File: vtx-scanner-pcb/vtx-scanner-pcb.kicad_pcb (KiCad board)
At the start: 2 copper layers, 24 parts, among them J1 Conn_01x06_Male, J2 Conn_01x08_Female, Q1 S8050, Q2 S8050, Q3 S8050, U1 RX5808, U2 AMS1117-3.3, U3 oskj-dc-dc, U4 AI-1027-TWT

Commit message: Started laying out PCB
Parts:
- added J3: SMA-J-P-H-RA-TH1, deets:SAMTEC_SMA-J-P-H-RA-TH1, B.Cu at (57.8, 40.8)
- added REF**: SSD1306, deets:SSD1306, F.Cu at (87.0, 46.4)
- C1, C2, C3, J1, J2, R1, R2, R3, U2, U3, U4: moved to B.Cu
- Q1, Q2, Q3: value S8050 -> MMSS8050-H-TP; footprint Package_TO_SOT_THT:TO-92_Inline -> digikey-footprints:SOT-23-3; moved to B.Cu
- S1, S2, S3, S4: value B3F-1000 -> FSM4JSMATR; footprint digikey-footprints:Switch_Tactile_THT_B3F-1xxx -> deets:Switch_Tactile_SMD_6x6mm
- moved U4 91.7 mm to (109.9, 39.4), turned to 180 degrees
- moved J2 76.2 mm to (94.6, 64.1), turned to 90 degrees
- moved Q3 68.6 mm to (112.4, 46.8), turned to 90 degrees
- moved A1 67.9 mm to (102.2, 78.1), turned to 90 degrees
- moved R7 63.7 mm to (94.6, 72.6), turned to 90 degrees
- moved R5 63.6 mm to (77.5, 72.8), turned to 90 degrees
- moved R6 62.5 mm to (77.5, 82.3), turned to 270 degrees
- moved R1 53.6 mm to (81.2, 131.2)
- moved C3 45.6 mm to (103.8, 91.4)
- moved R4 41.5 mm to (94.6, 82.3), turned to 270 degrees
- moved U2 37.8 mm to (96.5, 94.6), turned to 180 degrees
- moved C2 33.6 mm to (92.9, 143.3)
- moved R2 29.9 mm to (102.5, 105.9)
- moved U1 28.0 mm to (82.2, 48.5), turned to 0 degrees
- moved S1 26.5 mm to (85.7, 83.8)
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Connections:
- Q1 pad 1: /RTS -> Net-(Q1-Pad1)
- Q1 pad 2: Net-(Q1-Pad2) -> /RTS
- Q2 pad 1: /DTR -> Net-(Q2-Pad1)
- Q2 pad 2: Net-(Q2-Pad2) -> /DTR
- Q3 pad 1: -BATT -> /BUZZER
- Q3 pad 2: /BUZZER -> -BATT
- R1 pad 2: Net-(Q1-Pad2) -> Net-(Q1-Pad1)
- R2 pad 2: Net-(Q2-Pad2) -> Net-(Q2-Pad1)
- U1 pad 1: -BATT -> GNDA
- U1 pad 2: Net-(U1-Pad2) -> /ANT
- U1 pad 3: -BATT -> GNDA
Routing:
- net +5V: track 0.00 -> 136.9 mm, vias 0 -> 2
- net -BATT: track 0.00 -> 109.1 mm, vias 0 -> 1
- net /BUTTON_LEFT: track 0.00 -> 44.0 mm, vias 0 -> 1
- net /BUTTON_UP: track 0.00 -> 31.7 mm, vias 0 -> 1
- net /BUZZER: track 0.00 -> 25.3 mm
- net /BUTTON_DOWN: track 0.00 -> 24.5 mm, vias 0 -> 1
- net +3V3: track 0.00 -> 15.0 mm, vias 0 -> 1
- net GNDA: track 0.00 -> 13.3 mm
- net /ANT: track 0.00 -> 9.22 mm
- net /BUTTON_RIGHT: track 0.00 -> 9.10 mm
- net Net-(Q3-Pad3): track 0.00 -> 6.37 mm
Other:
- net class +5V added: clearance 0.2, trace_width 1.778, via_dia 0.8, via_drill 0.4
- net class GNDA_NN added: clearance 0.2, trace_width 0.75, via_dia 0.8, via_drill 0.4

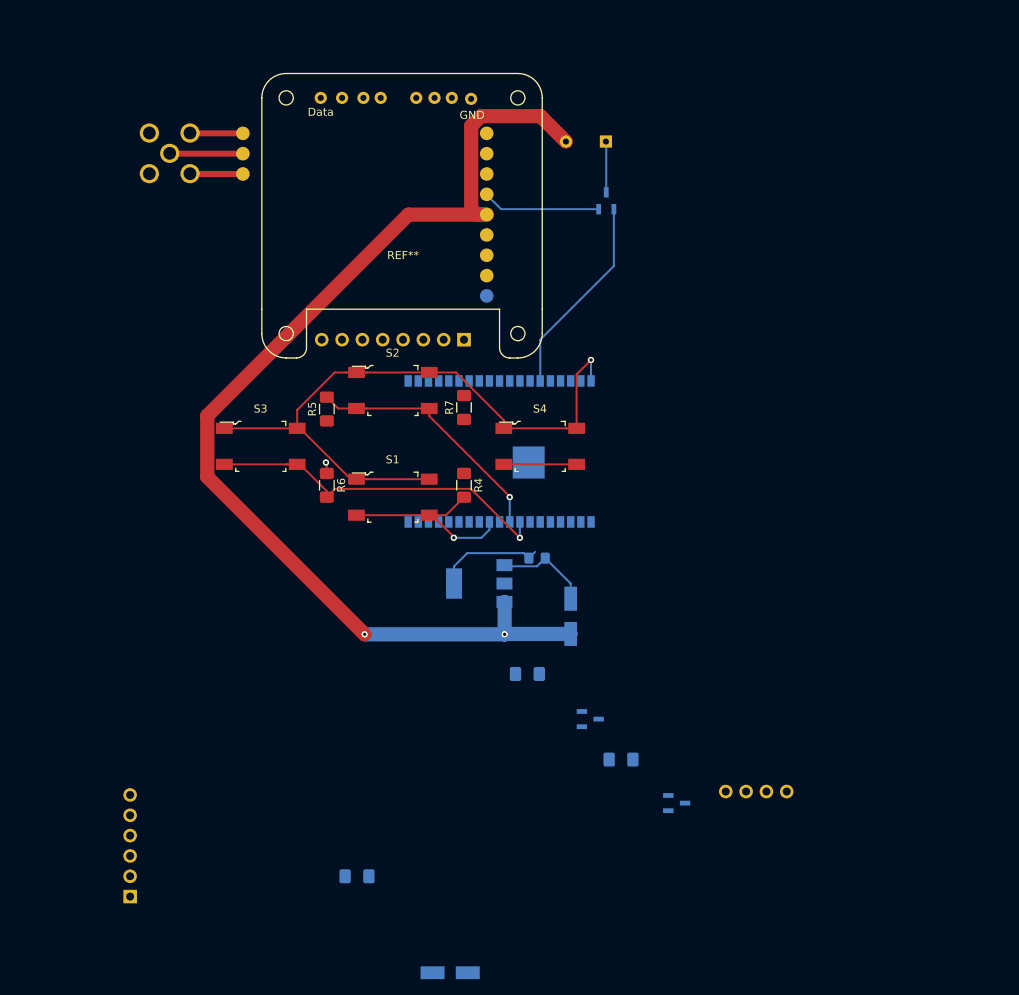
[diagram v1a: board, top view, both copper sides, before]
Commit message: Fully laid-out 4 layer PCB, the first!
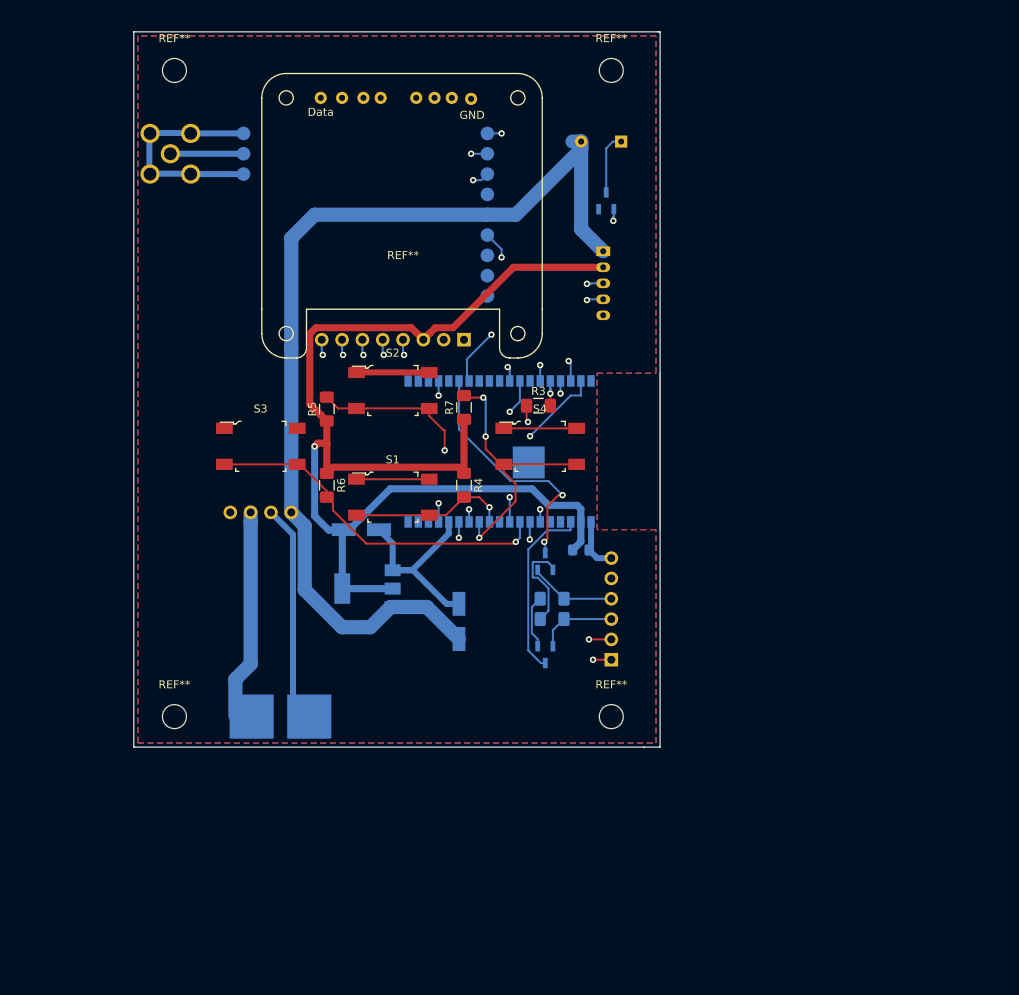
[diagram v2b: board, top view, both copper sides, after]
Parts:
- added J4: Conn_01x05, Connector_JST:JST_PH_S5B-PH-K_1x05_P2.00mm_Horizontal, B.Cu at (112.0, 53.1)
- added J5: XT60-M, deets:AMASS_XT60-M-SIDE-MOUNT, B.Cu at (71.7, 111.3)
- added REF**: MountingHole_3mm, MountingHole:MountingHole_3mm, F.Cu at (58.4, 30.5)
- added REF**: MountingHole_3mm, MountingHole:MountingHole_3mm, F.Cu at (113.0, 30.5)
- added REF**: MountingHole_3mm, MountingHole:MountingHole_3mm, F.Cu at (113.0, 111.3)
- added REF**: MountingHole_3mm, MountingHole:MountingHole_3mm, F.Cu at (58.4, 111.3)
- R3: moved to F.Cu
- moved J1 67.0 mm to (113.0, 104.1)
- moved U3 64.3 mm to (69.2, 94.6), turned to 180 degrees
- moved C2 56.5 mm to (81.8, 87.9)
- moved R3 45.4 mm to (103.9, 72.4)
- moved R1 42.4 mm to (105.6, 96.5), turned to 180 degrees
- moved Q1 24.8 mm to (104.8, 103.5), turned to 270 degrees
- moved Q2 20.5 mm to (104.8, 91.9), turned to 90 degrees
- moved C1 14.0 mm to (94.0, 99.4)
- moved U2 14.0 mm to (82.5, 95.2)
- moved R2 7.52 mm to (105.6, 99.1), turned to 180 degrees
- moved C3 5.56 mm to (109.2, 90.4)
- moved U4 1.91 mm to (111.8, 39.4)
- moved J3 0.10 mm to (57.9, 40.9)
- moved U1 0.08 mm to (82.3, 48.5)
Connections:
- A1 pad 26: Net-(A1-Pad26) -> /EXP1
- A1 pad 7: Net-(A1-Pad7) -> /EXP2
- J3 pad 2: GNDA -> -BATT
- J3 pad 3: GNDA -> -BATT
- J3 pad 4: GNDA -> -BATT
- J3 pad 5: GNDA -> -BATT
- U1 pad 1: GNDA -> -BATT
- U1 pad 3: GNDA -> -BATT
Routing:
- net +3V3: track 15.0 -> 151.7 mm
- net /VRX_DATA: track 0.00 -> 59.2 mm, vias 0 -> 2
- net /VRX_CS: track 0.00 -> 54.3 mm, vias 0 -> 2
- net /VRX_CLOCK: track 0.00 -> 46.6 mm, vias 0 -> 2
- net /SSD1306_DATA: track 0.00 -> 43.0 mm, vias 0 -> 2
- net /RX: track 0.00 -> 41.5 mm, vias 0 -> 2
- net /VRX_RSSI: track 0.00 -> 38.6 mm, vias 0 -> 2
- net /EXP2: track 0.00 -> 37.2 mm, vias 0 -> 2
- net /TX: track 0.00 -> 35.2 mm, vias 0 -> 2
- net /IO0: track 0.00 -> 30.9 mm, vias 0 -> 2
- net /SSD1306_CLK: track 0.00 -> 30.1 mm, vias 0 -> 2
- net +BATT: track 0.00 -> 26.2 mm
- net /BUTTON_RIGHT: track 9.10 -> 34.9 mm, vias 0 -> 3
- net /SSD1306_CS: track 0.00 -> 25.4 mm, vias 0 -> 2
- net /EXP1: track 0.00 -> 23.8 mm, vias 0 -> 2
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- added copper zone on B.Cu, net -BATT
- added copper zone on F.Cu, net -BATT
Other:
- board outline added: 65.8 x 89.4 mm
- copper layers 2 -> 4
- net class +3.3V added: clearance 0.2, trace_width 0.889, via_dia 0.8, via_drill 0.4

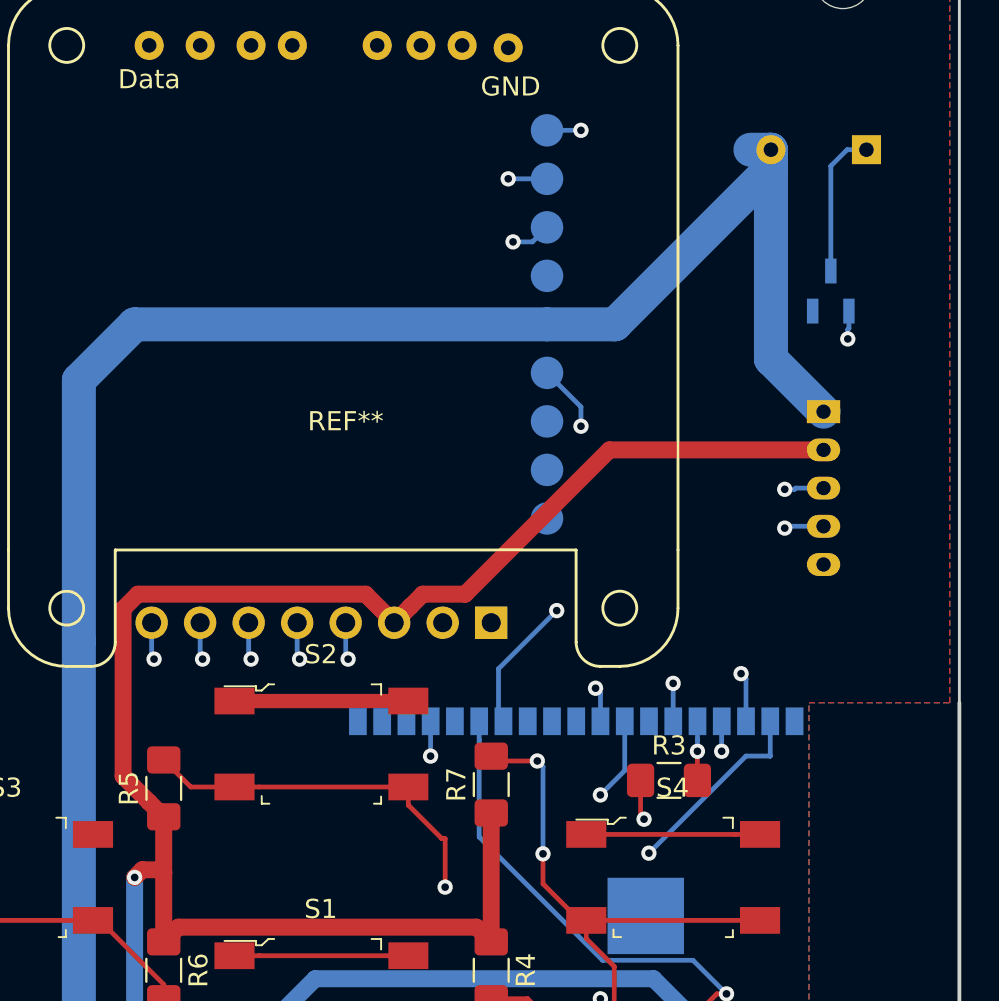
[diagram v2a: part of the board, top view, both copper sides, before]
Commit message: Re-organised a couple of power lines
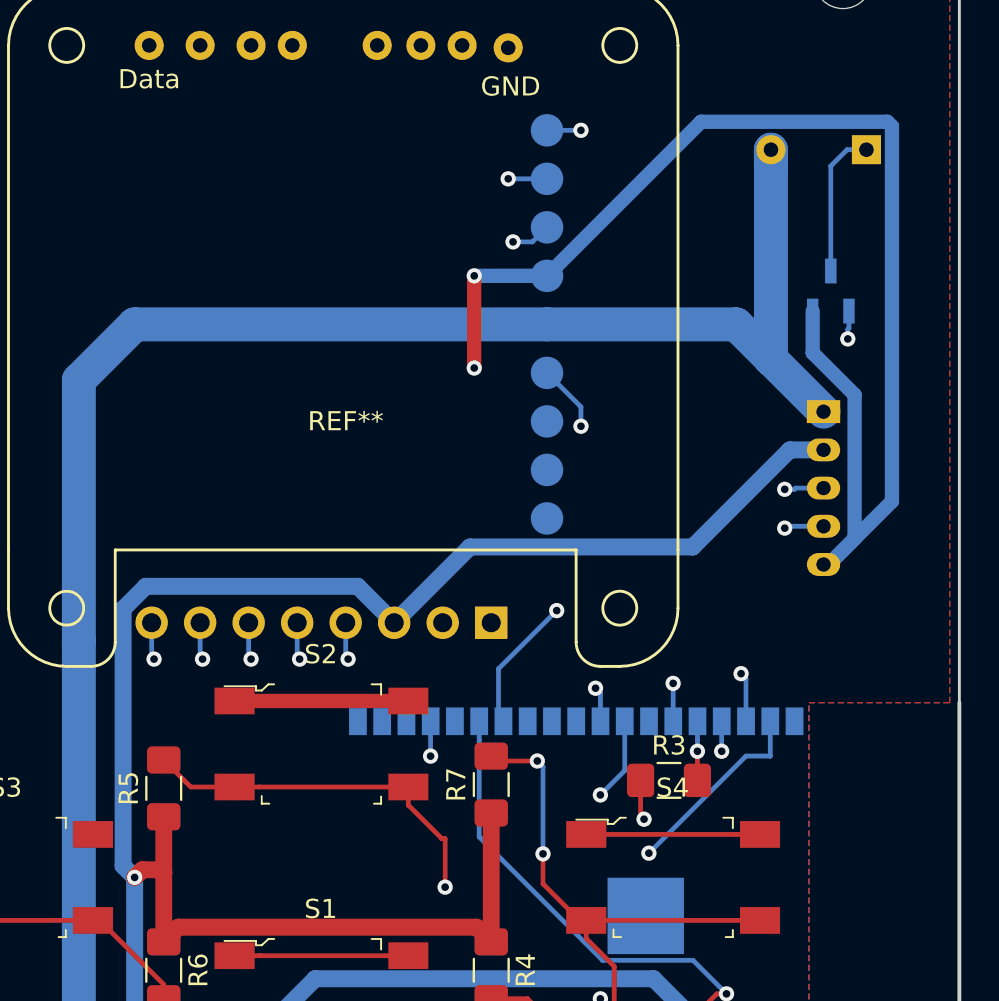
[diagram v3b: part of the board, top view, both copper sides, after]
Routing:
- net -BATT: track 116.7 -> 186.1 mm, vias 0 -> 2
- net +5V: track 126.3 -> 122.6 mm
- net +3V3: track 151.7 -> 154.6 mm

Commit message: Continue re-layouting
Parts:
- added CON1: SJ-3523-SMT-TR, deets:Switch_Slide_11.6x4mm_SJ-3523-SMT, F.Cu at (112.8, 41.7)
- added REF**: MountingHole_2.2mm_M2_DIN965, MountingHole:MountingHole_2.2mm_M2_DIN965, F.Cu at (72.4, 63.3)
- added REF**: MountingHole_2.2mm_M2_DIN965, MountingHole:MountingHole_2.2mm_M2_DIN965, F.Cu at (101.3, 63.4)
- added REF**: MountingHole_2.2mm_M2_DIN965, MountingHole:MountingHole_2.2mm_M2_DIN965, F.Cu at (72.4, 33.9)
- added REF**: MountingHole_2.2mm_M2_DIN965, MountingHole:MountingHole_2.2mm_M2_DIN965, F.Cu at (101.3, 33.9)
- A1, C3, Q3: moved to F.Cu
- moved C3 62.9 mm to (72.1, 39.6), turned to 90 degrees
- moved U4 55.4 mm to (58.4, 54.6), turned to 270 degrees
- moved Q3 47.4 mm to (65.0, 47.9), turned to 270 degrees
- moved A1 40.5 mm to (84.8, 41.5), turned to 0 degrees
- moved C2 33.8 mm to (58.4, 63.5), turned to 90 degrees
- moved C1 33.6 mm to (62.9, 86.7)
- moved U2 32.0 mm to (58.4, 74.3), turned to 90 degrees
- moved J1 27.6 mm to (86.4, 97.0), turned to 270 degrees
- moved R3 23.1 mm to (106.0, 95.4), turned to 90 degrees
- moved Q1 18.7 mm to (99.4, 85.5), turned to 180 degrees
- moved REF** 16.8 mm to (113.0, 94.5)
- moved REF** 16.8 mm to (58.4, 94.5)
- moved R2 12.8 mm to (103.9, 86.4), turned to 90 degrees
- moved J5 11.5 mm to (72.7, 99.8)
- moved U3 10.6 mm to (72.4, 84.5), turned to 0 degrees
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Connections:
- A1 pad 14: /VRX_DATA -> /VRX_CLOCK
- A1 pad 16: /VRX_CLOCK -> /VRX_DATA
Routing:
- net +3V3: track 154.6 -> 21.8 mm, vias 1 -> 7
- net -BATT: track 186.1 -> 57.5 mm, vias 2 -> 14
- net /SSD1306_DATA: track 43.0 -> 0.00 mm, vias 2 -> 0
- net /RX: track 41.5 -> 0.00 mm, vias 2 -> 0
- net +5V: track 122.6 -> 162.5 mm
- net /TX: track 35.2 -> 3.45 mm, vias 2 -> 0
- net /VRX_DATA: track 59.2 -> 27.4 mm
- net /IO0: track 30.9 -> 0.00 mm, vias 2 -> 0
- net /SSD1306_CLK: track 30.1 -> 0.00 mm, vias 2 -> 0
- net /VRX_CS: track 54.3 -> 24.7 mm, vias 2 -> 4
- net /BUTTON_LEFT: track 44.3 -> 14.9 mm, vias 1 -> 0
- net Net-(CON1-Pad2): track 0.00 -> 28.9 mm, vias 0 -> 2
- net /BUZZER: track 25.6 -> 0.00 mm, vias 2 -> 0
- net /SSD1306_CS: track 25.4 -> 0.00 mm, vias 2 -> 0
- net /#EN: track 22.7 -> 0.00 mm
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- added copper zone on In2.Cu, net +3V3
- removed copper zone on F.Cu, net -BATT
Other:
- board size 65.8 x 89.4 mm -> 65.8 x 77.2 mm

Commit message: re-layout finished
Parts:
- removed the REF** at (87.0, 46.4)
- CON1: moved to B.Cu
- moved R6 4.12 mm to (73.7, 83.9), turned to 90 degrees
- moved C3 1.91 mm to (73.7, 38.5)
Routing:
- net /RX: track 0.00 -> 83.7 mm
- net /#EN: track 0.00 -> 77.3 mm, vias 0 -> 2
- net /BUTTON_DOWN: track 15.7 -> 82.5 mm
- net Net-(A1-Pad34): track 0.00 -> 66.0 mm, vias 0 -> 2
- net /BUTTON_RIGHT: track 20.0 -> 67.7 mm
- net /IO0: track 0.00 -> 45.9 mm, vias 0 -> 3
- net /BUTTON_LEFT: track 14.9 -> 56.0 mm
- net /BUZZER: track 0.00 -> 40.6 mm, vias 0 -> 4
- net /SSD1306_DATA: track 0.00 -> 39.7 mm
- net /BUTTON_UP: track 13.4 -> 47.9 mm
- net /SSD1306_CS: track 0.00 -> 32.8 mm, vias 0 -> 2
- net /SSD1306_CLK: track 0.00 -> 29.5 mm
- net /SSD1306_RST: track 0.00 -> 25.9 mm, vias 0 -> 2
- net /SSD1306_DC: track 0.00 -> 21.4 mm, vias 0 -> 2
- net -BATT: track 57.5 -> 75.7 mm, vias 14 -> 29
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- added copper zone on B.Cu, net +3V3
- added copper zone on In2.Cu, net -BATT
- removed copper zone on In2.Cu, net +3V3
- removed copper zone on B.Cu, net -BATT
